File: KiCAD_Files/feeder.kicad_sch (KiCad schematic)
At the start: 39 parts, among them U702 TPS562202, U703 VPS8701B, U704 VPS8701B, U707 LMR38020SDDAR

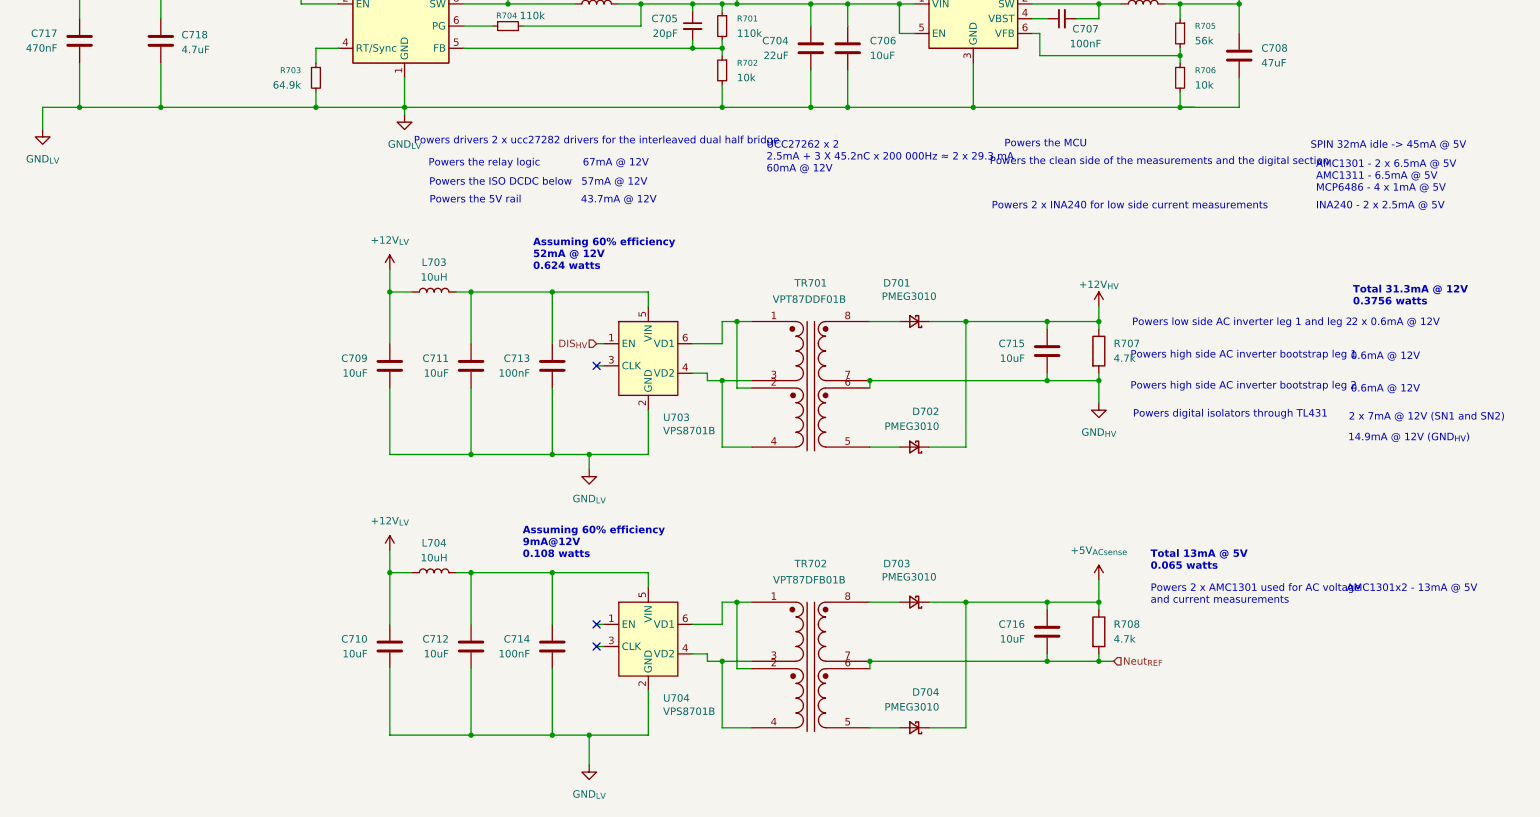
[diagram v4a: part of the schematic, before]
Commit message: Added TL431 for AC measurement 5V regulation. Added more film capacitance. Increased size of 100V ceramic caps to 1210.
Signed-off-by: Jean Alinei <jean.alinei@owntech.org>
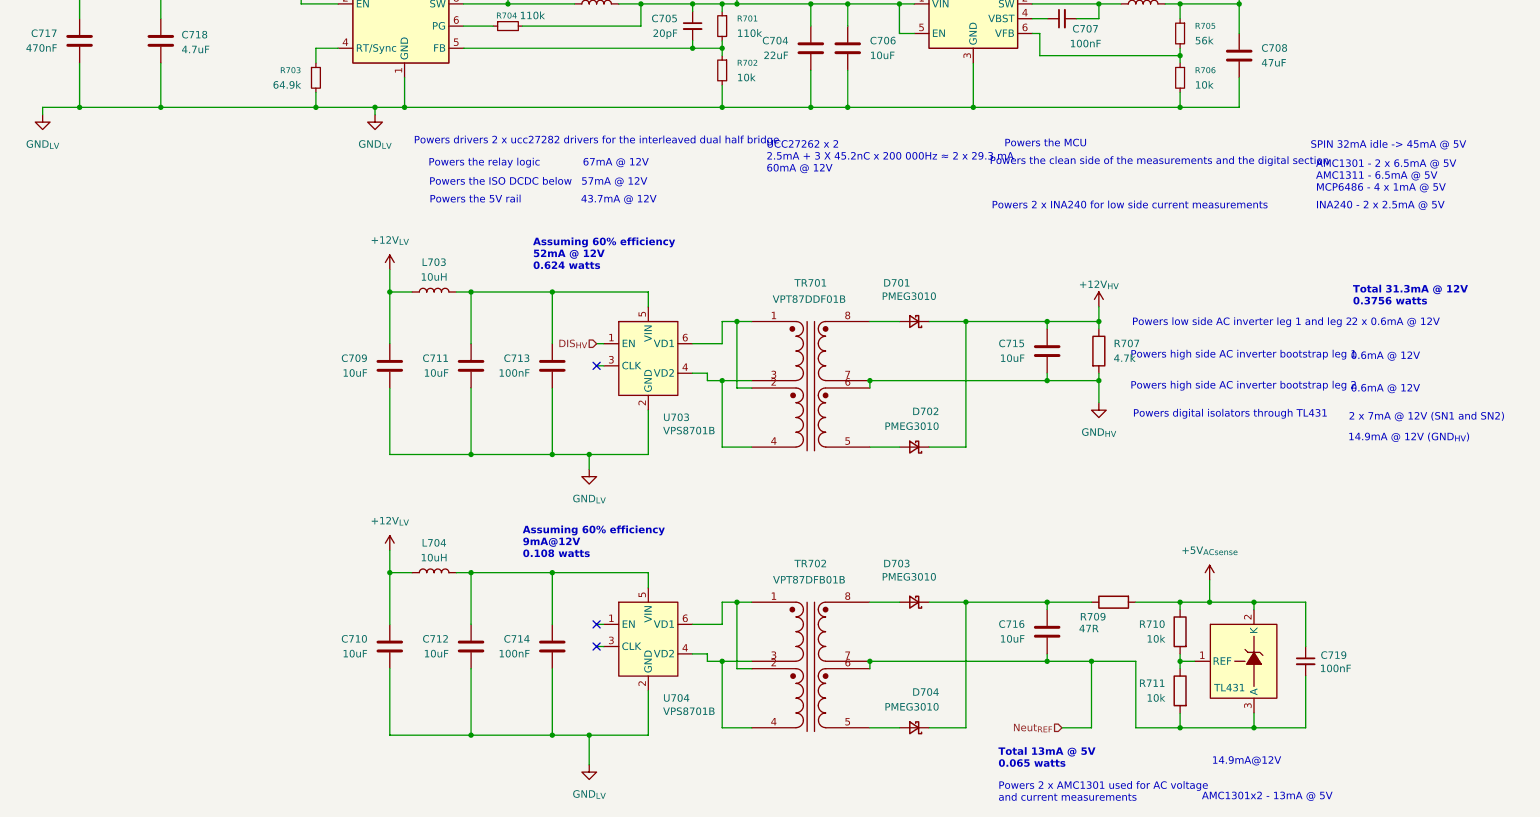
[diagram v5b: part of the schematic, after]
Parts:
- removed R708: 4.7k, Resistor_SMD:R_0603_1608Metric, symbol Device:R
- added C719: 100nF, Capacitor_SMD:C_0805_2012Metric, symbol Device:C_Small
- added R709: 47R, Resistor_SMD:R_0805_2012Metric, symbol Device:R
- added R710, R711: 10k, Resistor_SMD:R_0805_2012Metric, symbol Device:R
- added U705: TL431, Package_TO_SOT_SMD:SOT-23, symbol Symbols:TL431
- TR702: LCSC C2846915 -> C2846916
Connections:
- net +5V_{ACsense}: now also C719.1, R709.2, R710.1, U705.2 (K); no longer C716.1, D703.1 (K), D704.1 (K)
- net Neut_{REF}: now also C719.2, R711.2, U705.3 (A)
- new net: R710.2, R711.1, U705.1 (REF)
- new net: C716.1, D703.1 (K), D704.1 (K), R709.1
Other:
- note added: "14.9mA@12V"

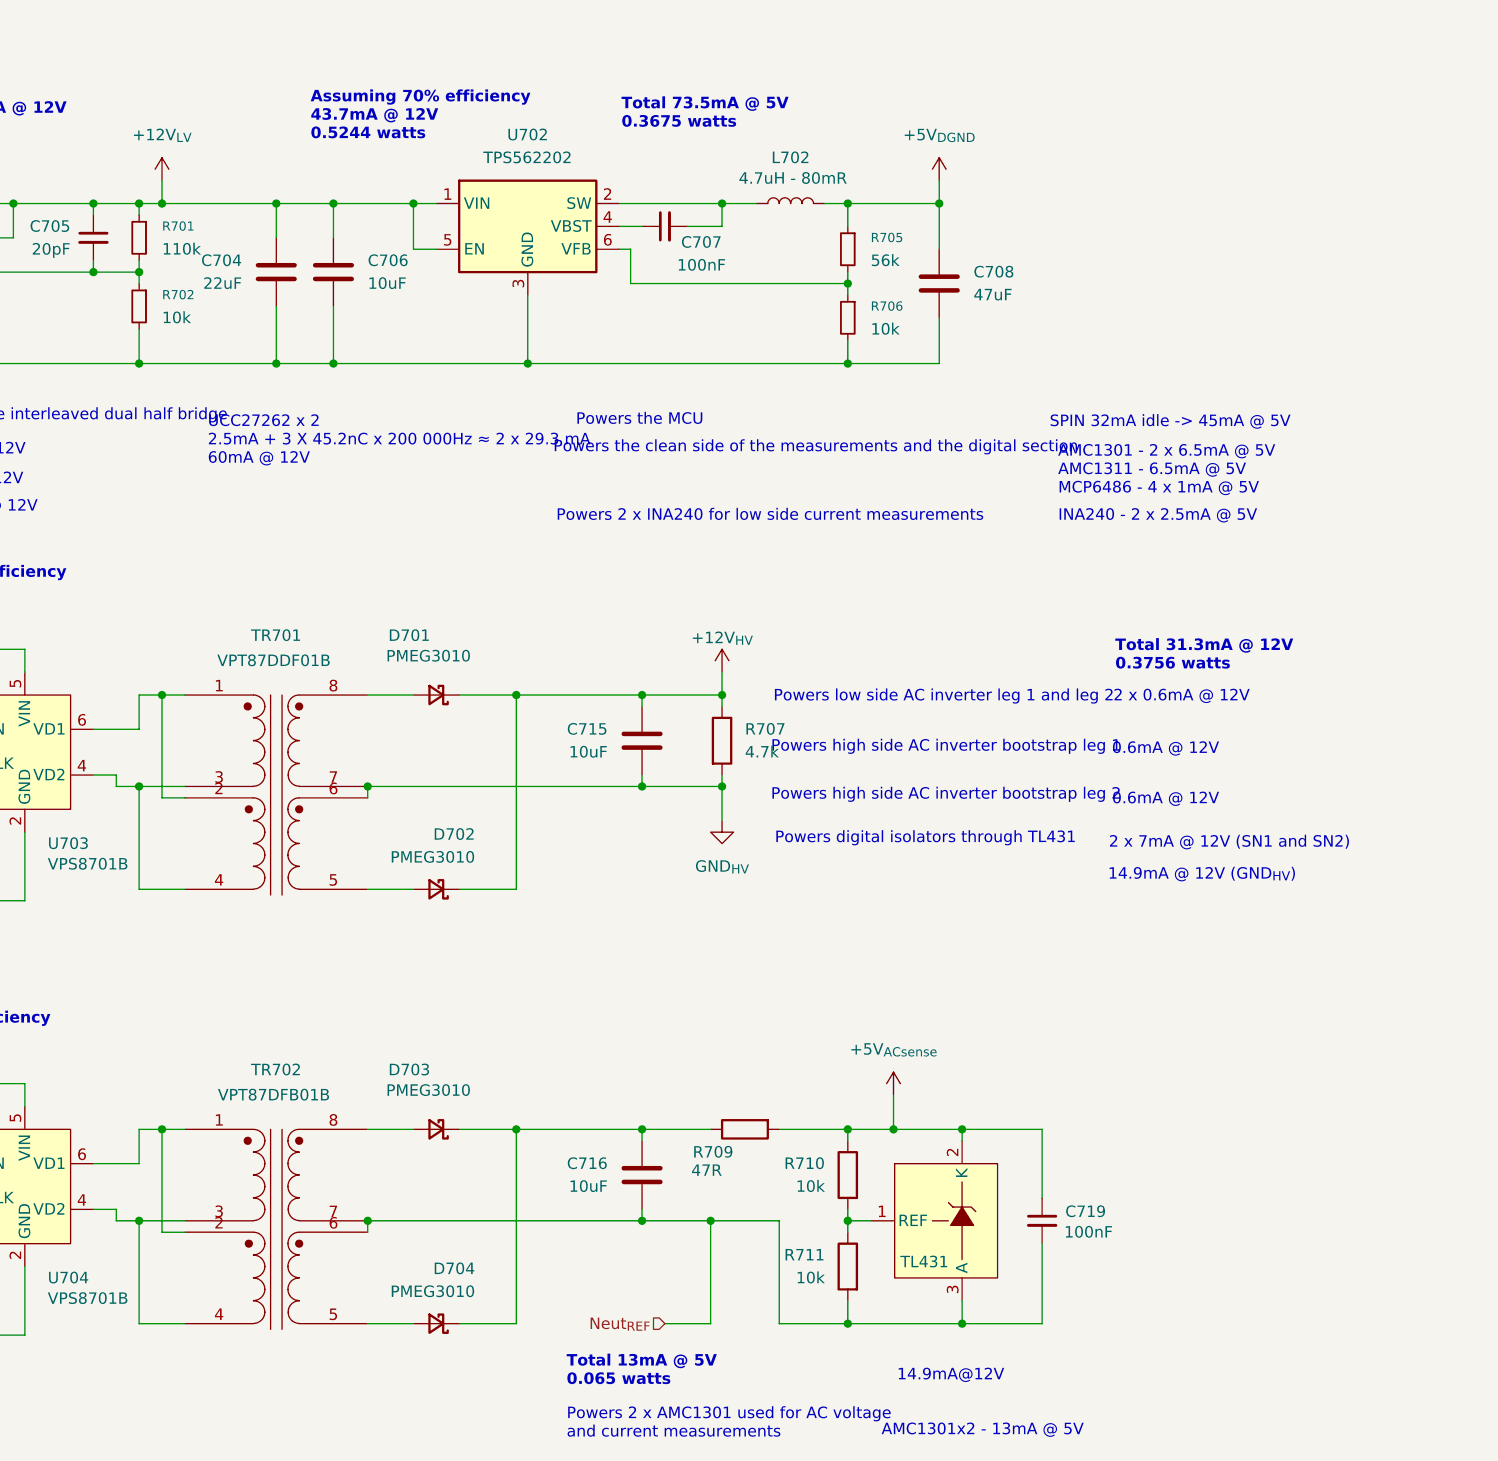
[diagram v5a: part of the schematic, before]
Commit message: V0.9 as ordered 23/01/26. Improved silkscreen, added 1nF on enable pin signals.
Signed-off-by: Jean Alinei <jean.alinei@owntech.org>
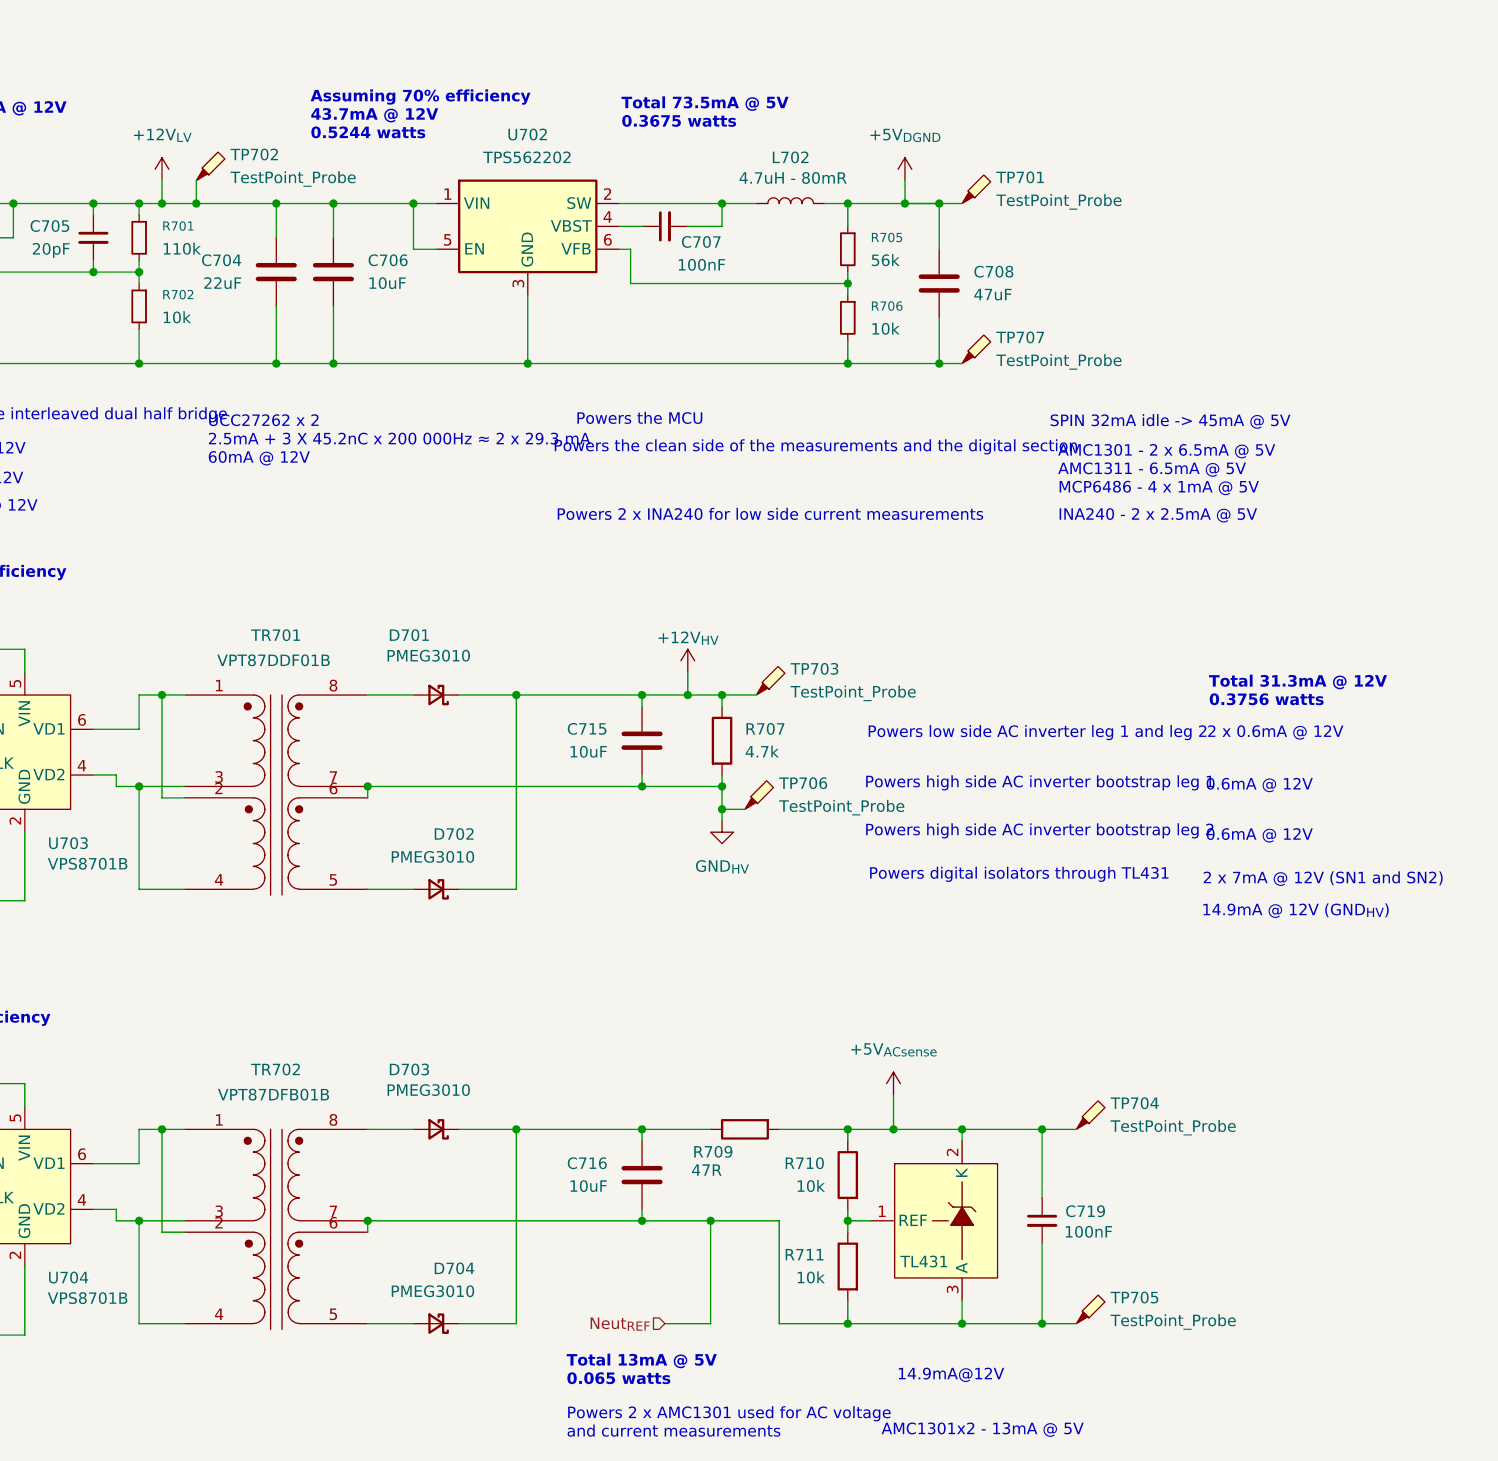
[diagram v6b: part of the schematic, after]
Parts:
- added TP701, TP702, TP703, TP704, TP705, TP706, TP707: TestPoint_Probe, TestPoint:TestPoint_Pad_D1.0mm, symbol Connector:TestPoint_Probe
- R709: LCSC C17710 -> C17714
- TR702: LCSC C2846916 -> C2846915
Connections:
- net +12V_{HV}: now also TP703.1
- net +12V_{LV}: now also TP702.1
- net +5V_{ACsense}: now also TP704.1
- net +5V_{DGND}: now also TP701.1
- net GND_{HV}: now also TP706.1
- net GND_{LV}: now also TP707.1
- net Neut_{REF}: now also TP705.1

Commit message: Tidied up the schematic. Added the pdf version for V0.9.
Signed-off-by: Jean Alinei <jean.alinei@owntech.org>
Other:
- title: (none) -> Internal power supplies
- moved on the sheet: C703, C704, C705, C706, C707, C708, C709, C710, C711, C712, C713, C714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

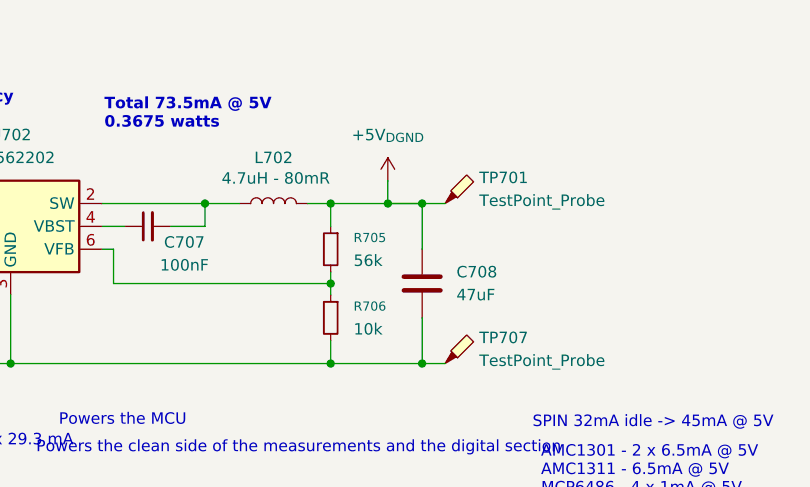
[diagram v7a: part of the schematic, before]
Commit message: Modified the differential inductor filter footprints slightly. Solves #2.
Signed-off-by: Jean Alinei <jean.alinei@owntech.org>
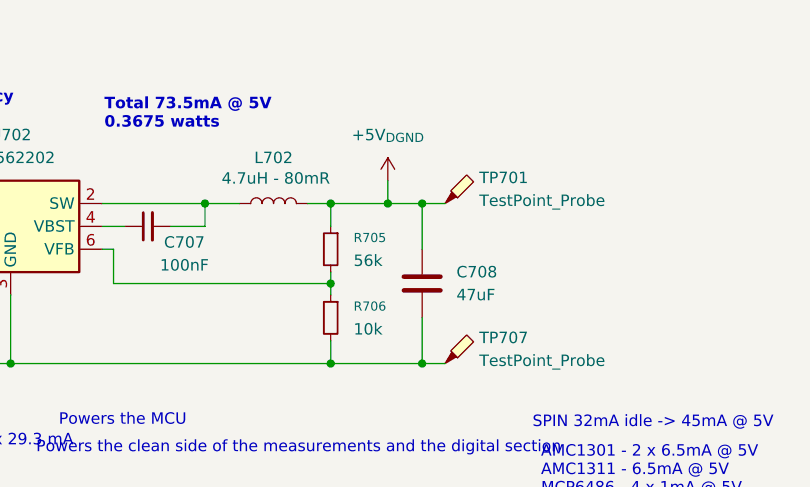
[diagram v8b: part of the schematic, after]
